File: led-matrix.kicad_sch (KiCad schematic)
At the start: 69 parts, among them J1 Touch Pad x4, U1 MAX7219, U1 Pico

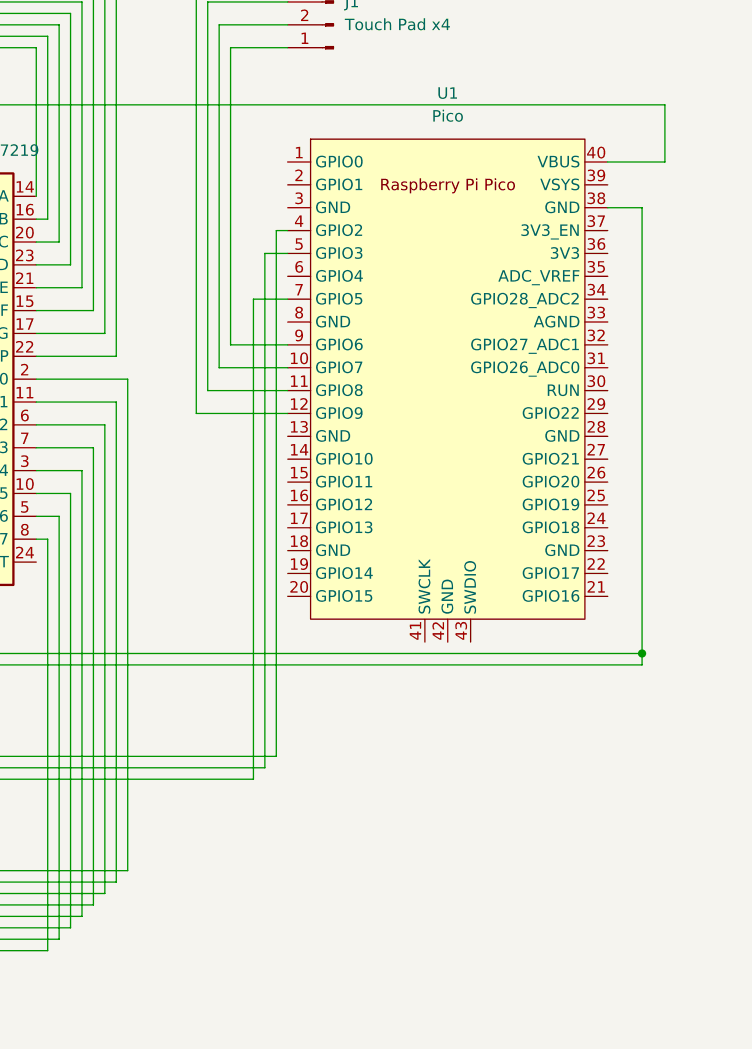
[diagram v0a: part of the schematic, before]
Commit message: feat: add gpio breakout
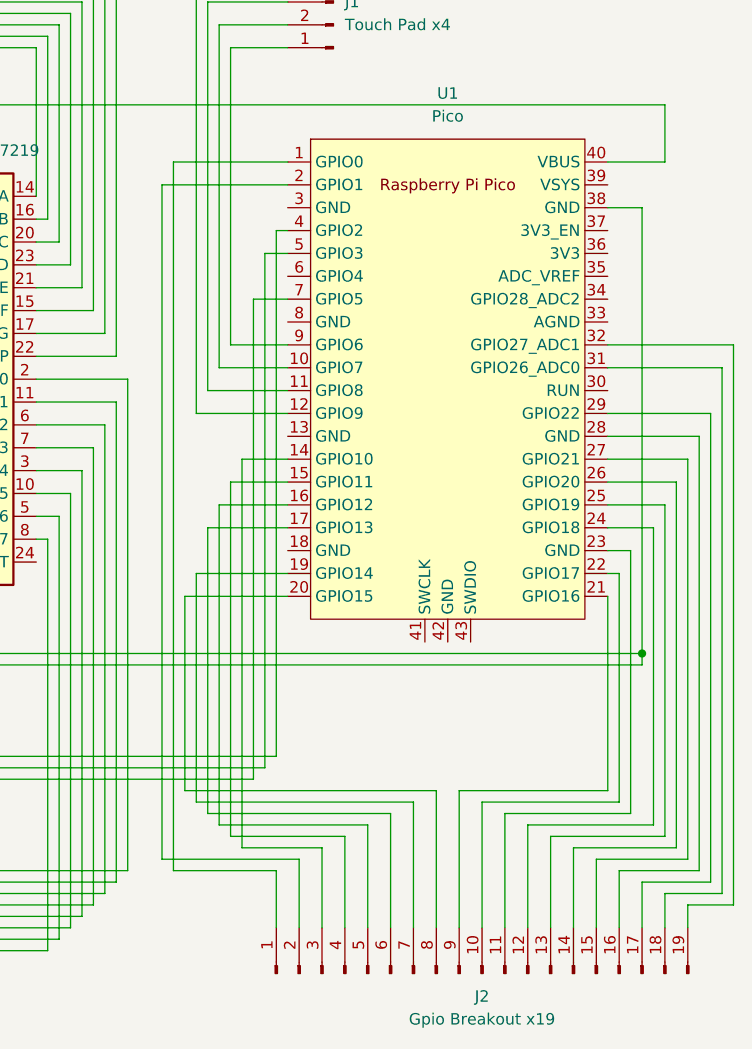
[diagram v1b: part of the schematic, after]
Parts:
- added J2: Gpio Breakout x19, symbol Connector:Conn_01x19_Pin
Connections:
- net at U1.1 (GPIO0): now also J2.1 (Pin_1)
- net at U1.14 (GPIO10): now also J2.3 (Pin_3)
- net at U1.15 (GPIO11): now also J2.4 (Pin_4)
- net at U1.16 (GPIO12): now also J2.5 (Pin_5)
- net at U1.17 (GPIO13): now also J2.6 (Pin_6)
- net at U1.19 (GPIO14): now also J2.7 (Pin_7)
- net at U1.2 (GPIO1): now also J2.2 (Pin_2)
- net at U1.20 (GPIO15): now also J2.8 (Pin_8)
- net at U1.21 (GPIO16): now also J2.9 (Pin_9)
- net at U1.22 (GPIO17): now also J2.10 (Pin_10)
- net at U1.23 (GND): now also J2.11 (Pin_11)
- net at U1.24 (GPIO18): now also J2.12 (Pin_12)
- net at U1.25 (GPIO19): now also J2.13 (Pin_13)
- net at U1.26 (GPIO20): now also J2.14 (Pin_14)
- net at U1.27 (GPIO21): now also J2.15 (Pin_15)
- net at U1.28 (GND): now also J2.16 (Pin_16)
- net at U1.29 (GPIO22): now also J2.17 (Pin_17)
- net at U1.31 (GPIO26_ADC0): now also J2.18 (Pin_18)
- net at U1.32 (GPIO27_ADC1): now also J2.19 (Pin_19)

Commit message: feat: add pico footprint and max7219
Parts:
- removed J1: Touch Pad x4, symbol Connector:Conn_01x04_Pin
- removed J2: Gpio Breakout x19, symbol Connector:Conn_01x19_Pin
- added J1, J10, J11, J12, J13, J14, J15, J16, J17, J18, J19, J2, J20, J21, J22, J23, J3, J4, J5, J6, J7, J8, J9: Conn_01x01_Pin, Connector_Pin:Pin_D1.2mm_L11.3mm_W3.0mm_Flat, symbol Connector:Conn_01x01_Pin
- C1: footprint (none) -> Capacitor_THT:C_Axial_L3.8mm_D2.6mm_P7.50mm_Horizontal
- D1, D10, D11, D12, D13, D14, D15, D16, D17, D18, D19, D2, D20, D21, D22, D23, D24, D25, D26, D27, D28, D29, D3, D30, D31, D32, D33, D34, D35, D36, D37, D38, D39, D4, D40, D41, D42, D43, D44, D45, D46, D47, D48, D49, D5, D50, D51, D52, D53, D54, D55, D56, D57, D58, D59, D6, D60, D61, D62, D63, D64, D7, D8, D9: footprint (none) -> LED_THT:LED_D3.0mm_Clear
- R1: footprint (none) -> Resistor_THT:R_Axial_DIN0204_L3.6mm_D1.6mm_P1.90mm_Vertical
- U1: footprint (none) -> max7219:DIL24
- U2: renamed from U1; footprint RPi_Pico:RPi_Pico_SMD_TH -> MCU_RaspberryPi_and_Boards:RPi_Pico_SMD_TH
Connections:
- net at U2.1 (GPIO0): now also J2.1 (Pin_1)
- net at U2.10 (GPIO7): now also J4.1 (Pin_1)
- net at U2.11 (GPIO8): now also J3.1 (Pin_1)
- net at U2.12 (GPIO9): now also J1.1 (Pin_1)
- net at U2.14 (GPIO10): now also J7.1 (Pin_1)
- net at U2.15 (GPIO11): now also J8.1 (Pin_1)
- net at U2.16 (GPIO12): now also J9.1 (Pin_1)
- net at U2.17 (GPIO13): now also J10.1 (Pin_1)
- net at U2.19 (GPIO14): now also J11.1 (Pin_1)
- net at U2.2 (GPIO1): now also J6.1 (Pin_1)
- net at U2.20 (GPIO15): now also J12.1 (Pin_1)
- net at U2.21 (GPIO16): now also J13.1 (Pin_1)
- net at U2.22 (GPIO17): now also J14.1 (Pin_1)
- net at U2.23 (GND): now also J15.1 (Pin_1)
- net at U2.24 (GPIO18): now also J16.1 (Pin_1)
- net at U2.25 (GPIO19): now also J17.1 (Pin_1)
- net at U2.26 (GPIO20): now also J18.1 (Pin_1)
- net at U2.27 (GPIO21): now also J19.1 (Pin_1)
- net at U2.28 (GND): now also J20.1 (Pin_1)
- net at U2.29 (GPIO22): now also J21.1 (Pin_1)
- net at U2.31 (GPIO26_ADC0): now also J22.1 (Pin_1)
- net at U2.32 (GPIO27_ADC1): now also J23.1 (Pin_1)
- net at U2.9 (GPIO6): now also J5.1 (Pin_1)

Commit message: chore: make resister bigger and align max7219 and cap / resister
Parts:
- R1: footprint Resistor_THT:R_Axial_DIN0204_L3.6mm_D1.6mm_P1.90mm_Vertical -> Resistor_THT:R_Axial_DIN0204_L3.6mm_D1.6mm_P7.62mm_Horizontal
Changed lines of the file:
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@@
 			)
 		)
-		(property "Footprint" "Resistor_THT:R_Axial_DIN0204_L3.6mm_D1.6mm_P1.90mm_Vertical"
+		(property "Footprint" "Resistor_THT:R_Axial_DIN0204_L3.6mm_D1.6mm_P7.62mm_Horizontal"
 			(at 169.418 43.18 90)
 			(effects
